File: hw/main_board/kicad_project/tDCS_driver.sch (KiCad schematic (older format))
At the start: 57 parts, among them P1 CONN_5, P2 CONN_5, P3 CONN_6, P4 CONN_8, P5 CONN_8, U1 MAX338, U2 SI5351A, U3 AD5292, U4 AD8221, U5 MAX339, U6 OP1177, U7 MAX338, X1 CRYSTAL6-10pf

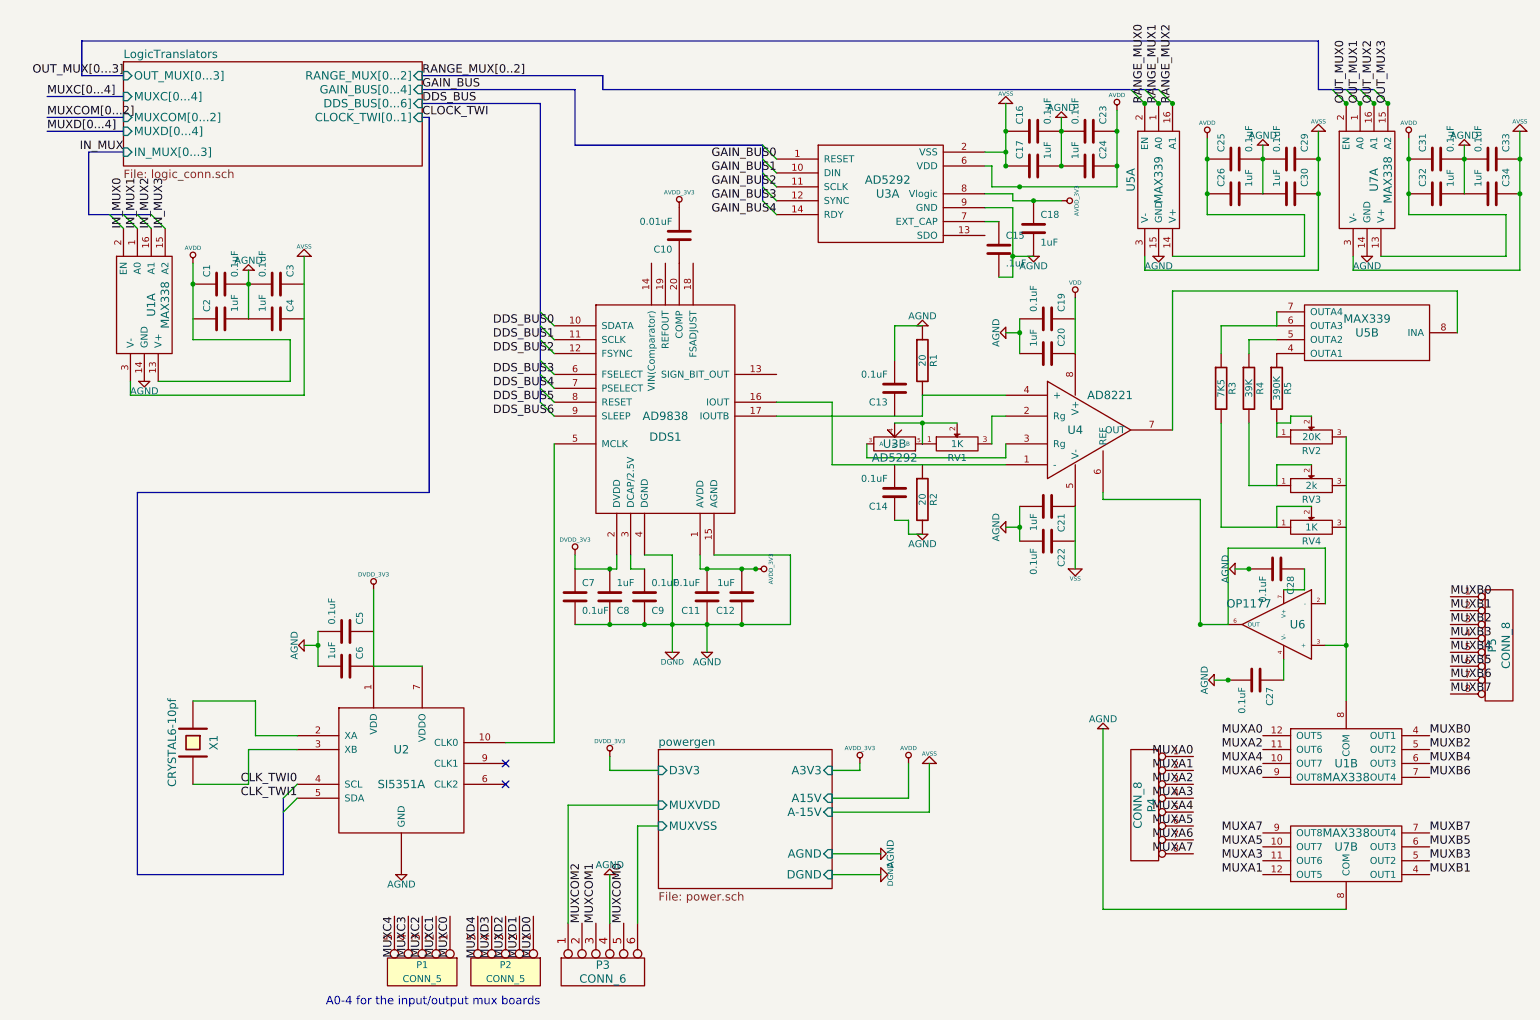
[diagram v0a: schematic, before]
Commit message: refactored schematic, finalized gain/range
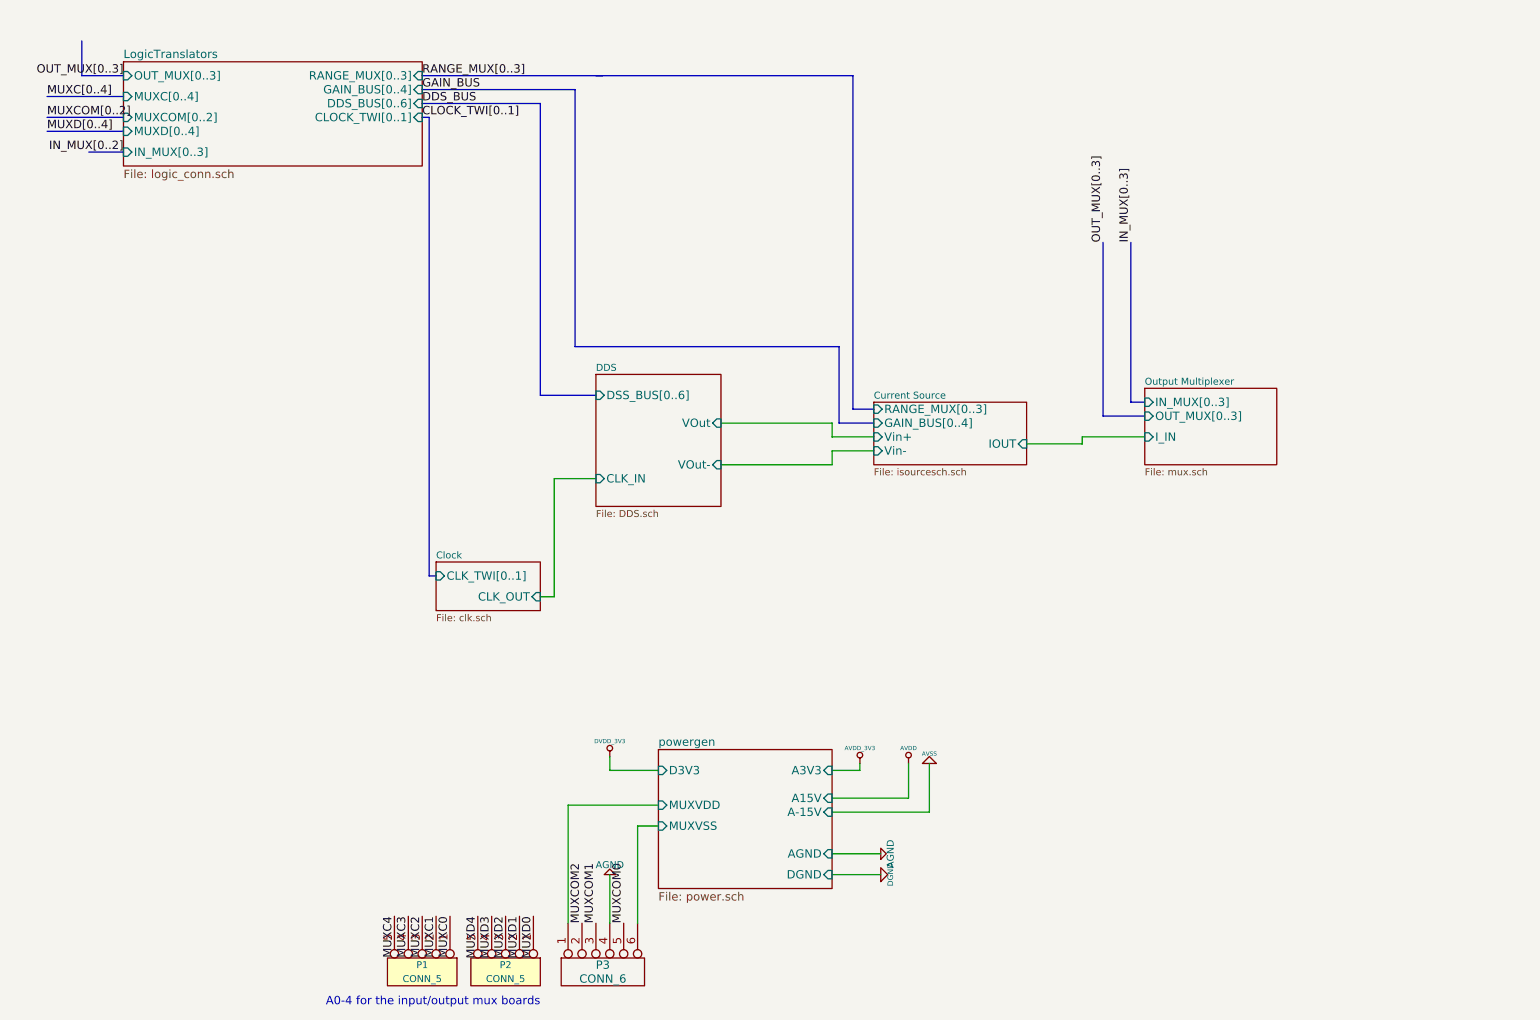
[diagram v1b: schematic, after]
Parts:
- removed C1, C11, C13, C14, C16, C19, C22, C23, C25, C27, C28, C29, C3, C31, C33, C5, C7, C9: 0.1uF, symbol C
- removed C10: 0.01uF, symbol C
- removed C12, C17, C18, C2, C20, C21, C24, C26, C30, C32, C34, C4, C6, C8: 1uF, symbol C
- removed C15: .1uF, symbol C
- removed DDS1: AD9838, symbol AD9838
- removed P4, P5: CONN_8, symbol CONN_8
- removed R1, R2: 20, symbol R
- removed R3: 7K5, symbol R
- removed R4: 39K, symbol R
- removed R5: 390K, symbol R
- removed RV1, RV4: 1K, symbol POT
- removed RV2: 20K, symbol POT
- removed RV3: 2k, symbol POT
- removed U1, U7: MAX338, symbol MAX338
- removed U2: SI5351A, symbol SI5351A
- removed U3: AD5292, symbol AD5292
- removed U4: AD8221, symbol AD8221
- removed U5: MAX339, symbol MAX339
- removed U6: OP1177, symbol OP1177
- removed X1: CRYSTAL6-10pf, symbol CRYSTAL
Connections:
- no-connect marks 2 -> 0

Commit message: started mainboard pcb layout, fixing small things in schematic, TODO: schematic connector symbols and pads
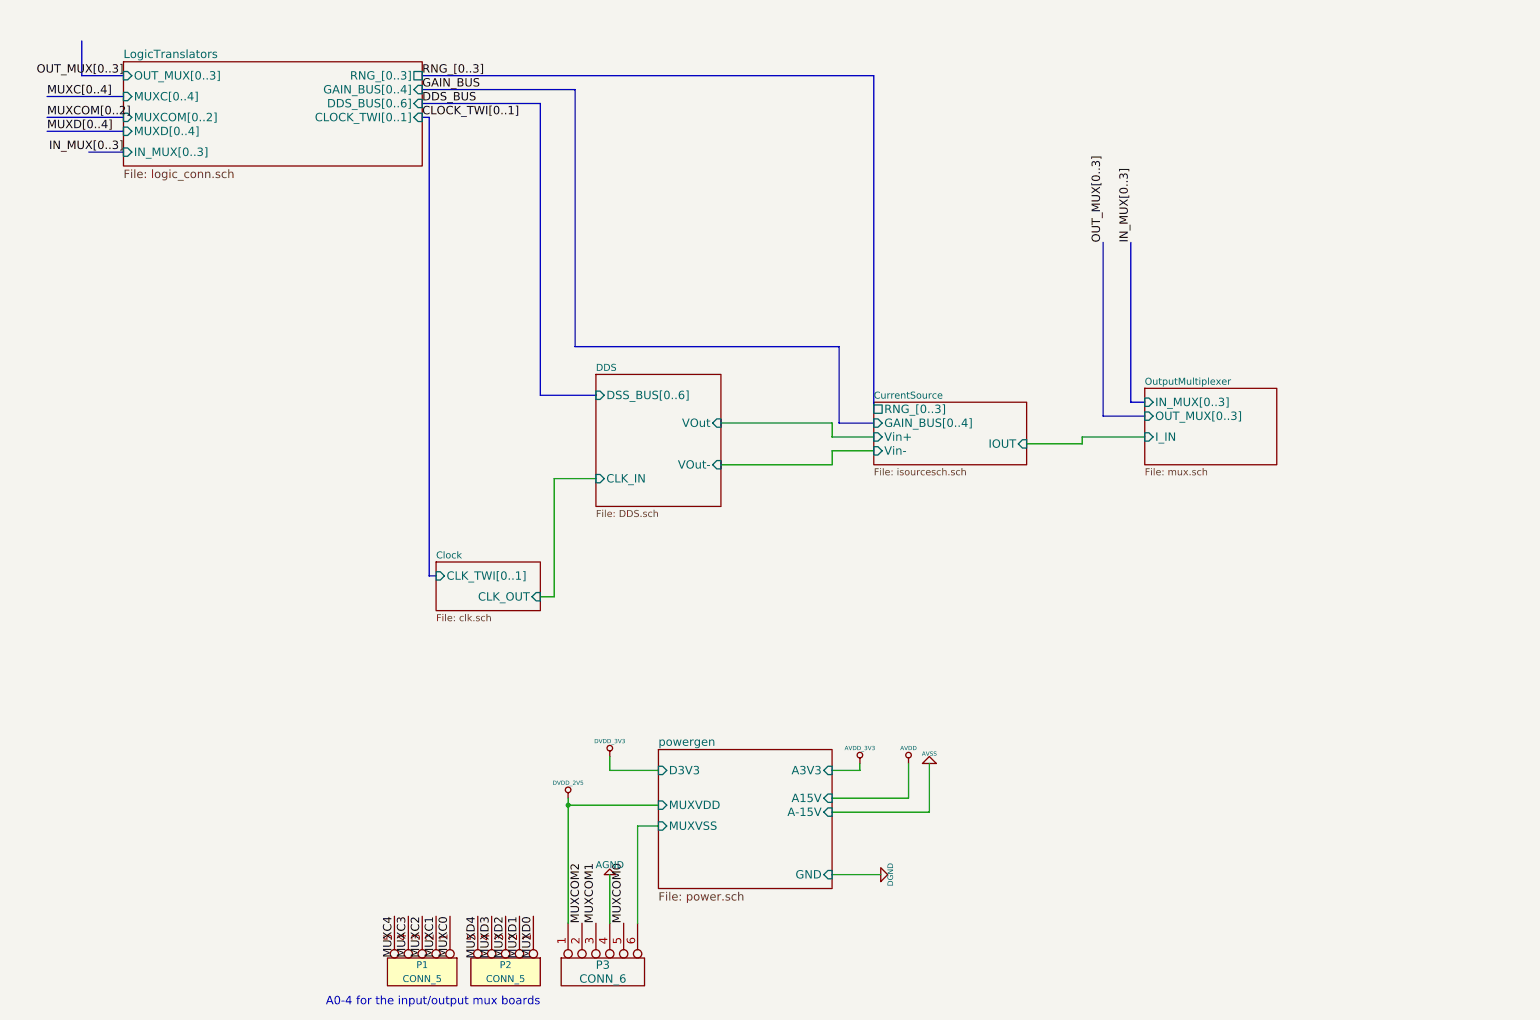
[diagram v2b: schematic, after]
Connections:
- net powergen/MUXVDD renamed DVDD_2V5
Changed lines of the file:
@@
 encoding utf-8
 Sheet 1 7
-Title "noname.sch"
-Date "26 feb 2014"
-Rev ""
+Title "tDCS current driver"
+Date "01 Feb 2014"
+Rev "A"
 Comp ""
-Comment1 ""
+Comment1 "Copyright 2014 Andrey Shmakov"
 Comment2 ""
 Comment3 ""
@@
 $EndComp
 $Comp
-L DVDD_3V3 #PWR08
+L DVDD_3V3 #PWR02
 U 1 1 52266045
 P 4600 6000
-F 0 "#PWR08" H 4600 6100 30  0001 C CNN
+F 0 "#PWR02" H 4600 6100 30  0001 C CNN
 F 1 "DVDD_3V3" H 4600 6110 30  0000 C CNN
 F 2 "" H 4600 6000 60  0001 C CNN
@@
 F3 "A-15V" I R 6200 6400 60
 F4 "A15V" I R 6200 6300 60
-F5 "AGND" I R 6200 6700 60
-F6 "MUXVDD" I L 4950 6350 60
-F7 "MUXVSS" I L 4950 6500 60
-F8 "D3V3" I L 4950 6100 60
-F9 "DGND" I R 6200 6850 60
-$EndSheet
-$Comp
-L AVDD_3V3 #PWR09
+F5 "MUXVDD" I L 4950 6350 60
+F6 "MUXVSS" I L 4950 6500 60
+F7 "D3V3" I L 4950 6100 60
+F8 "GND" I R 6200 6850 60
+$EndSheet
+$Comp
+L AVDD_3V3 #PWR03
 U 1 1 52265F6F
 P 6400 6050
-F 0 "#PWR09" H 6400 6150 30  0001 C CNN
+F 0 "#PWR03" H 6400 6150 30  0001 C CNN
 F 1 "AVDD_3V3" H 6400 6160 30  0000 C CNN
 F 2 "" H 6400 6050 60  0001 C CNN
@@
 MUXCOM1
 $Comp
-L AGND #PWR011
+L AGND #PWR04
 U 1 1 52265AC3
 P 4600 6850
-F 0 "#PWR011" H 4600 6850 40  0001 C CNN
+F 0 "#PWR04" H 4600 6850 40  0001 C CNN
 F 1 "AGND" H 4600 6780 50  0000 C CNN
 F 2 "" H 4600 6850 60  0001 C CNN
@@
 MUXCOM0
 $Comp
-L AGND #PWR027
-U 1 1 5217BD7F
-P 6550 6700
-F 0 "#PWR027" H 6550 6700 40  0001 C CNN
-F 1 "AGND" H 6550 6630 50  0000 C CNN
-F 2 "" H 6550 6700 60  0001 C CNN
-F 3 "" H 6550 6700 60  0001 C CNN
-	1    6550 6700
-	0    -1   -1   0
-$EndComp
-$Comp
-L AVDD #PWR028
+L AVDD #PWR05
 U 1 1 5217BC9E
 P 6750 6050
-F 0 "#PWR028" H 6750 6150 30  0001 C CNN
+F 0 "#PWR05" H 6750 6150 30  0001 C CNN
 F 1 "AVDD" H 6750 6160 30  0000 C CNN
 F 2 "" H 6750 6050 60  0001 C CNN
@@
 $EndComp
 $Comp
-L AVSS #PWR029
+L AVSS #PWR06
 U 1 1 5217BC95
 P 6900 6050
-F 0 "#PWR029" H 6900 6050 30  0001 C CNN
+F 0 "#PWR06" H 6900 6050 30  0001 C CNN
 F 1 "AVSS" H 6900 5980 30  0000 C CNN
 F 2 "" H 6900 6050 60  0001 C CNN
@@
 F2 "DDS_BUS[0..6]" I R 3250 1300 60
 F3 "CLOCK_TWI[0..1]" I R 3250 1400 60
-F4 "RANGE_MUX[0..3]" I R 3250 1100 60
-F5 "GAIN_BUS[0..4]" I R 3250 1200 60
-F6 "OUT_MUX[0..3]" I L 1100 1100 60
-F7 "IN_MUX[0..3]" I L 1100 1650 60
-F8 "MUXC[0..4]" I L 1100 1250 60
-F9 "MUXD[0..4]" I L 1100 1500 60
-F10 "MUXCOM[0..2]" I L 1100 1400 60
+F4 "GAIN_BUS[0..4]" I R 3250 1200 60
+F5 "OUT_MUX[0..3]" I L 1100 1100 60
+F6 "IN_MUX[0..3]" I L 1100 1650 60
+F7 "MUXC[0..4]" I L 1100 1250 60
+F8 "MUXD[0..4]" I L 1100 1500 60
+F9 "MUXCOM[0..2]" I L 1100 1400 60
+F10 "RNG_[0..3]" U R 3250 1100 60
 $EndSheet
 Text Label 1100 1100 2    60   ~ 0
 OUT_MUX[0..3]
 Text Label 1100 1650 2    60   ~ 0
-IN_MUX[0..2]
+IN_MUX[0..3]
 Text Label 3250 1100 0    60   ~ 0
-RANGE_MUX[0..3]
+RNG_[0..3]
 Text Label 3250 1200 0    60   ~ 0
 GAIN_BUS
@@
 	4600 7200 4600 6850
 Wire Wire Line
-	4300 6350 4300 7200
+	4300 6300 4300 7200
 Wire Wire Line
 	4950 6350 4300 6350
@@
 Wire Bus Line
 	3250 1200 4350 1200
-Wire Bus Line
-	4550 1100 3250 1100
-Wire Wire Line
-	6550 6700 6200 6700
 Wire Wire Line
 	6750 6300 6750 6050
@@
 S 6500 3450 1100 450
 U 531699F6
-F0 "Current Source" 50
+F0 "CurrentSource" 50
 F1 "isourcesch.sch" 50
 F2 "Vin+" I L 6500 3700 60
 F3 "Vin-" I L 6500 3800 60
-F4 "RANGE_MUX[0..3]" I L 6500 3500 60
+F4 "RNG_[0..3]" U L 6500 3500 60
 F5 "IOUT" I R 7600 3750 60
 F6 "GAIN_BUS[0..4]" I L 6500 3600 60
@@
 Wire Bus Line
 	6250 3600 6500 3600
-Wire Bus Line
-	6500 3500 6350 3500
-Wire Bus Line
-	6350 3500 6350 1100
-Wire Bus Line
-	6350 1100 4500 1100
 $Sheet
 S 8450 3350 950  550
 U 531703E6
-F0 "Output Multiplexer" 50
+F0 "OutputMultiplexer" 50
 F1 "mux.sch" 50
 F2 "IN_MUX[0..3]" I L 8450 3450 60
@@
 Text Label 8150 2300 1    60   ~ 0
 OUT_MUX[0..3]
+$Comp
+L DVDD_2V5 #PWR07
+U 1 1 5318760A
+P 4300 6300
+F 0 "#PWR07" H 4300 6400 30  0001 C CNN
+F 1 "DVDD_2V5" H 4300 6410 30  0000 C CNN
+F 2 "" H 4300 6300 60  0000 C CNN
+F 3 "" H 4300 6300 60  0000 C CNN
+	1    4300 6300
+	1    0    0    -1
+$EndComp
+Connection ~ 4300 6350
+Wire Bus Line
+	6500 3500 6500 1100
+Wire Bus Line
+	6500 1100 3250 1100
 $EndSCHEMATC

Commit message: finished component layout on mainboard, need to route power planes and the digital control signal lines
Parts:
- removed P1, P2: CONN_5, symbol CONN_5
- removed P3: CONN_6, symbol CONN_6
- added P14, P15: CONN_5X2, symbol CONN_5X2
- added P16: CONN_3X2, symbol CONN_3X2
- added P17, P18: CONN_2X2, symbol CONN_2X2
- added SCREW1, SCREW2, SCREW3, SCREW4: CONN_1, symbol CONN_1
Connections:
- net labels added: MUXVDD, MUXVSS
- wire segments 26 -> 24
- no-connect marks 0 -> 4
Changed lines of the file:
@@
 EESchema Schematic File Version 2
 LIBS:ddslib
+LIBS:demuxcomplib
 LIBS:tDCS_driver-cache
 EELAYER 24 0
@@
 	1    0    0    -1
 $EndComp
-Text Label 3650 7150 3    60   ~ 0
-MUXD4
-Text Label 3750 7150 3    60   ~ 0
-MUXD3
-Text Label 3850 7150 3    60   ~ 0
-MUXD2
-Text Label 3950 7150 3    60   ~ 0
-MUXD1
-Text Label 4050 7150 3    60   ~ 0
-MUXD0
-Text Label 3050 7150 3    60   ~ 0
-MUXC4
-Text Label 3150 7150 3    60   ~ 0
-MUXC3
-Text Label 3250 7150 3    60   ~ 0
-MUXC2
-Text Label 3350 7150 3    60   ~ 0
-MUXC1
-Text Label 3450 7150 3    60   ~ 0
-MUXC0
 Text Label 550  1500 0    60   ~ 0
 MUXD[0..4]
@@
 Text Label 550  1250 0    60   ~ 0
 MUXC[0..4]
-Text Label 4500 7200 1    60   ~ 0
-MUXCOM1
-$Comp
-L AGND #PWR04
-U 1 1 52265AC3
-P 4600 6850
-F 0 "#PWR04" H 4600 6850 40  0001 C CNN
-F 1 "AGND" H 4600 6780 50  0000 C CNN
-F 2 "" H 4600 6850 60  0001 C CNN
-F 3 "" H 4600 6850 60  0001 C CNN
-	1    4600 6850
-	-1   0    0    1
-$EndComp
 Text Notes 4100 7800 2    60   ~ 0
 A0-4 for the input/output mux boards
 $Comp
-L CONN_5 P1
-U 1 1 52265826
-P 3250 7550
-F 0 "P1" V 3200 7550 50  0000 C CNN
-F 1 "CONN_5" V 3300 7550 50  0000 C CNN
-F 2 "" H 3250 7550 60  0001 C CNN
-F 3 "" H 3250 7550 60  0001 C CNN
-	1    3250 7550
-	0    1    1    0
-$EndComp
-$Comp
-L CONN_5 P2
-U 1 1 52265825
-P 3850 7550
-F 0 "P2" V 3800 7550 50  0000 C CNN
-F 1 "CONN_5" V 3900 7550 50  0000 C CNN
-F 2 "" H 3850 7550 60  0001 C CNN
-F 3 "" H 3850 7550 60  0001 C CNN
-	1    3850 7550
-	0    1    1    0
-$EndComp
-$Comp
-L CONN_6 P3
-U 1 1 52265824
-P 4550 7550
-F 0 "P3" V 4500 7550 60  0000 C CNN
-F 1 "CONN_6" V 4600 7550 60  0000 C CNN
-F 2 "" H 4550 7550 60  0001 C CNN
-F 3 "" H 4550 7550 60  0001 C CNN
-	1    4550 7550
-	0    -1   1    0
-$EndComp
-Text Label 4400 7200 1    60   ~ 0
-MUXCOM2
-Text Label 4700 7200 1    60   ~ 0
-MUXCOM0
-$Comp
-L AVDD #PWR05
+L AVDD #PWR04
 U 1 1 5217BC9E
 P 6750 6050
-F 0 "#PWR05" H 6750 6150 30  0001 C CNN
+F 0 "#PWR04" H 6750 6150 30  0001 C CNN
 F 1 "AVDD" H 6750 6160 30  0000 C CNN
 F 2 "" H 6750 6050 60  0001 C CNN
@@
 $EndComp
 $Comp
-L AVSS #PWR06
+L AVSS #PWR05
 U 1 1 5217BC95
 P 6900 6050
-F 0 "#PWR06" H 6900 6050 30  0001 C CNN
+F 0 "#PWR05" H 6900 6050 30  0001 C CNN
 F 1 "AVSS" H 6900 5980 30  0000 C CNN
 F 2 "" H 6900 6050 60  0001 C CNN
@@
 	1100 1400 550  1400
 Wire Wire Line
-	4600 7200 4600 6850
-Wire Wire Line
-	4300 6300 4300 7200
-Wire Wire Line
 	4950 6350 4300 6350
 Wire Bus Line
@@
 Wire Bus Line
 	850  1650 1100 1650
-Wire Wire Line
-	4800 6500 4800 7200
 Wire Wire Line
 	4950 6500 4800 6500
@@
 OUT_MUX[0..3]
 $Comp
-L DVDD_2V5 #PWR07
+L DVDD_2V5 #PWR06
 U 1 1 5318760A
 P 4300 6300
-F 0 "#PWR07" H 4300 6400 30  0001 C CNN
+F 0 "#PWR06" H 4300 6400 30  0001 C CNN
 F 1 "DVDD_2V5" H 4300 6410 30  0000 C CNN
 F 2 "" H 4300 6300 60  0000 C CNN
@@
 Wire Bus Line
 	6500 1100 3250 1100
+$Comp
+L CONN_5X2 P15
+U 1 1 5327C208
+P 1250 5850
+F 0 "P15" H 1250 6150 60  0000 C CNN
+F 1 "CONN_5X2" V 1250 5850 50  0000 C CNN
+F 2 "" H 1250 5850 60  0000 C CNN
+F 3 "" H 1250 5850 60  0000 C CNN
+	1    1250 5850
+	-1   0    0    -1
+$EndComp
+$Comp
+L CONN_5X2 P14
+U 1 1 5327C217
+P 2950 5700
+F 0 "P14" H 2950 6000 60  0000 C CNN
+F 1 "CONN_5X2" V 2950 5700 50  0000 C CNN
+F 2 "" H 2950 5700 60  0000 C CNN
+F 3 "" H 2950 5700 60  0000 C CNN
+	1    2950 5700
+	1    0    0    1
+$EndComp
+$Comp
+L CONN_2X2 P18
+U 1 1 5327C2DA
+P 1300 7200
+F 0 "P18" H 1300 7350 50  0000 C CNN
+F 1 "CONN_2X2" H 1310 7070 40  0000 C CNN
+F 2 "" H 1300 7200 60  0000 C CNN
+F 3 "" H 1300 7200 60  0000 C CNN
+	1    1300 7200
+	-1   0    0    -1
+$EndComp
+$Comp
+L CONN_2X2 P17
+U 1 1 5327C2E9
+P 2200 6600
+F 0 "P17" H 2200 6750 50  0000 C CNN
+F 1 "CONN_2X2" H 2210 6470 40  0000 C CNN
+F 2 "" H 2200 6600 60  0000 C CNN
+F 3 "" H 2200 6600 60  0000 C CNN
+	1    2200 6600
+	1    0    0    -1
+$EndComp
+$Comp
+L CONN_3X2 P16
+U 1 1 5327C3AC
+P 3350 6400
+F 0 "P16" H 3350 6650 50  0000 C CNN
+F 1 "CONN_3X2" V 3350 6450 40  0000 C CNN
+F 2 "" H 3350 6400 60  0000 C CNN
+F 3 "" H 3350 6400 60  0000 C CNN
+	1    3350 6400
+	1    0    0    -1
+$EndComp
+Text Label 850  5650 2    60   ~ 0
+MUXC0
+Text Label 850  5750 2    60   ~ 0
+MUXC1
+Text Label 850  5850 2    60   ~ 0
+MUXC2
+Text Label 850  5950 2    60   ~ 0
+MUXC3
+Text Label 850  6050 2    60   ~ 0
+MUXC4
+Text Label 1650 5650 0    60   ~ 0
+MUXD0
+Text Label 1650 5750 0    60   ~ 0
+MUXD1
+Text Label 1650 5850 0    60   ~ 0
+MUXD2
+Text Label 1650 5950 0    60   ~ 0
+MUXD3
+Text Label 1650 6050 0    60   ~ 0
+MUXD4
+Text Label 2550 5500 2    60   ~ 0
+MUXC0
+Text Label 2550 5600 2    60   ~ 0
+MUXC1
+Text Label 2550 5700 2    60   ~ 0
+MUXC2
+Text Label 2550 5800 2    60   ~ 0
+MUXC3
+Text Label 2550 5900 2    60   ~ 0
+MUXC4
+Text Label 3350 5500 0    60   ~ 0
+MUXD0
+Text Label 3350 5600 0    60   ~ 0
+MUXD1
+Text Label 3350 5700 0    60   ~ 0
+MUXD2
+Text Label 3350 5800 0    60   ~ 0
+MUXD3
+Text Label 3350 5900 0    60   ~ 0
+MUXD4
+Text Label 2950 6250 2    60   ~ 0
+MUXCOM0
+Text Label 2950 6350 2    60   ~ 0
+MUXCOM1
+Text Label 2950 6450 2    60   ~ 0
+MUXCOM2
+Text Label 3750 6250 0    60   ~ 0
+MUXCOM2
+Text Label 3750 6350 0    60   ~ 0
+MUXCOM1
+Text Label 3750 6450 0    60   ~ 0
+MUXCOM0
+Text Label 1800 6550 2    60   ~ 0
+AGND
+Text Label 1800 6650 2    60   ~ 0
+AGND
+Text Label 2600 6550 0    60   ~ 0
+AGND
+Text Label 2600 6650 0    60   ~ 0
+AGND
+Text Label 900  7250 2    60   ~ 0
+MUXVDD
+Text Label 1700 7150 0    60   ~ 0
+MUXVSS
+Text Label 900  7150 2    60   ~ 0
+MUXVSS
+Text Label 1700 7250 0    60   ~ 0
+MUXVDD
+$Comp
+L CONN_1 SCREW1
+U 1 1 5328DC39
+P 1850 3850
+F 0 "SCREW1" H 1930 3850 40  0000 L CNN
+F 1 "CONN_1" H 1850 3905 30  0001 C CNN
+F 2 "" H 1850 3850 60  0000 C CNN
+F 3 "" H 1850 3850 60  0000 C CNN
+	1    1850 3850
+	1    0    0    -1
+$EndComp
+$Comp
+L CONN_1 SCREW2
+U 1 1 5328DEC1
+P 1850 3950
+F 0 "SCREW2" H 1930 3950 40  0000 L CNN
+F 1 "CONN_1" H 1850 4005 30  0001 C CNN
+F 2 "" H 1850 3950 60  0000 C CNN
+F 3 "" H 1850 3950 60  0000 C CNN
+	1    1850 3950
+	1    0    0    -1
+$EndComp
+$Comp
+L CONN_1 SCREW3
+U 1 1 5328DEC7
+P 1850 4050
+F 0 "SCREW3" H 1930 4050 40  0000 L CNN
+F 1 "CONN_1" H 1850 4105 30  0001 C CNN
+F 2 "" H 1850 4050 60  0000 C CNN
+F 3 "" H 1850 4050 60  0000 C CNN
+	1    1850 4050
+	1    0    0    -1
+$EndComp
+$Comp
+L CONN_1 SCREW4
+U 1 1 5328DECD
+P 1850 4150
+F 0 "SCREW4" H 1930 4150 40  0000 L CNN
+F 1 "CONN_1" H 1850 4205 30  0001 C CNN
+F 2 "" H 1850 4150 60  0000 C CNN
+F 3 "" H 1850 4150 60  0000 C CNN
+	1    1850 4150
+	1    0    0    -1
+$EndComp
+NoConn ~ 1700 3850
+NoConn ~ 1700 3950
+NoConn ~ 1700 4050
+NoConn ~ 1700 4150
+Wire Wire Line
+	4300 6350 4300 6300
 $EndSCHEMATC

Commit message: Converting keepnote notes to thorough design documentation, starting with BRD1
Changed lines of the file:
@@
 LIBS:ddslib
 LIBS:demuxcomplib
+LIBS:conn
 LIBS:tDCS_driver-cache
 EELAYER 24 0
@@
 Wire Wire Line
 	4300 6350 4300 6300
+Text Label 4550 6350 1    60   ~ 0
+MUXVDD
+Text Label 4800 6500 2    60   ~ 0
+MUXVSS
 $EndSCHEMATC
